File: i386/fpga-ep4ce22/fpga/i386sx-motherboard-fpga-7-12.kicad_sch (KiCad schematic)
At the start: 1 part, among them U3 (1/6) EP4CE22F17C8N

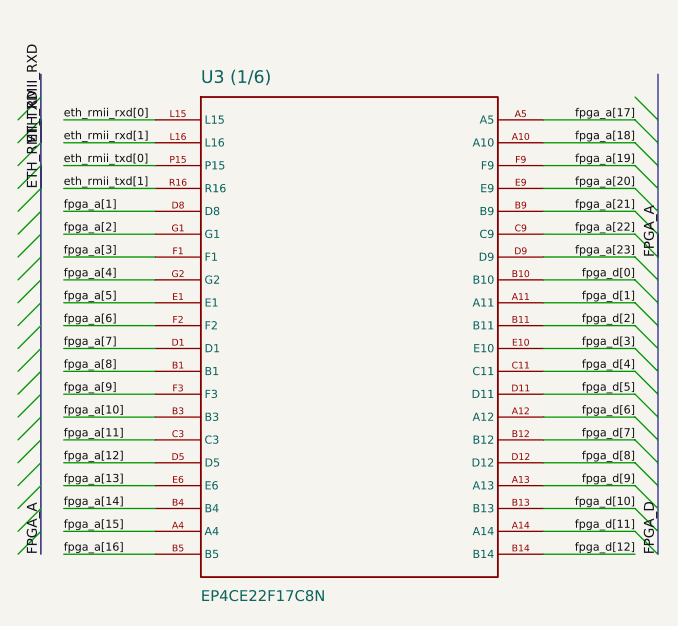
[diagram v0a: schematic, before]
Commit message: Publish the motherboards' KiCad files
From socket3@c0f6464 socket7@9205469 socket370@524f5b1 i386@bea926c
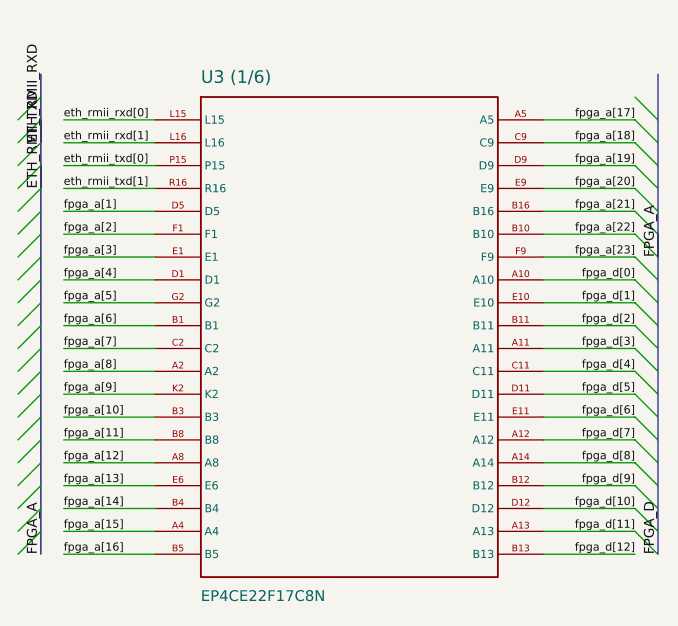
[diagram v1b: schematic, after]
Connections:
- net fpga_a[11]: now also U3 (1/6).B8; no longer U3 (1/6).C3
- net fpga_a[12]: now also U3 (1/6).A8; no longer U3 (1/6).D5
- net fpga_a[18]: now also U3 (1/6).C9; no longer U3 (1/6).A10
- net fpga_a[19]: now also U3 (1/6).D9; no longer U3 (1/6).F9
- net fpga_a[1]: now also U3 (1/6).D5; no longer U3 (1/6).D8
- net fpga_a[21]: now also U3 (1/6).B16; no longer U3 (1/6).B9
- net fpga_a[22]: now also U3 (1/6).B10; no longer U3 (1/6).C9
- net fpga_a[23]: now also U3 (1/6).F9; no longer U3 (1/6).D9
- net fpga_a[2]: now also U3 (1/6).F1; no longer U3 (1/6).G1
- net fpga_a[3]: now also U3 (1/6).E1; no longer U3 (1/6).F1
- net fpga_a[4]: now also U3 (1/6).D1; no longer U3 (1/6).G2
- net fpga_a[5]: now also U3 (1/6).G2; no longer U3 (1/6).E1
- net fpga_a[6]: now also U3 (1/6).B1; no longer U3 (1/6).F2
- net fpga_a[7]: now also U3 (1/6).C2; no longer U3 (1/6).D1
- net fpga_a[8]: now also U3 (1/6).A2; no longer U3 (1/6).B1
- net fpga_a[9]: now also U3 (1/6).K2; no longer U3 (1/6).F3
- net fpga_d[0]: now also U3 (1/6).A10; no longer U3 (1/6).B10
- net fpga_d[10]: now also U3 (1/6).D12; no longer U3 (1/6).B13
- net fpga_d[11]: now also U3 (1/6).A13; no longer U3 (1/6).A14
- net fpga_d[12]: now also U3 (1/6).B13; no longer U3 (1/6).B14
- net fpga_d[1]: now also U3 (1/6).E10; no longer U3 (1/6).A11
- net fpga_d[3]: now also U3 (1/6).A11; no longer U3 (1/6).E10
- net fpga_d[6]: now also U3 (1/6).E11; no longer U3 (1/6).A12
- net fpga_d[7]: now also U3 (1/6).A12; no longer U3 (1/6).B12
- net fpga_d[8]: now also U3 (1/6).A14; no longer U3 (1/6).D12
- net fpga_d[9]: now also U3 (1/6).B12; no longer U3 (1/6).A13
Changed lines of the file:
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@@
     (property "Reference" "U3 (1/6)" (at 44.46 17.65 0) (effects (font (size 1.4 1.4)) (justify left bottom)))
     (property "Value" "EP4CE22F17C8N" (at 44.46 73.79 0) (effects (font (size 1.2 1.2)) (justify left top)))
-    (instances (project "i386sx-motherboard" (path "/0ac398a9-1d89-4090-a36f-db7b4d3d6c0d/3610057a-4bad-4a42-9f8e-069125d0cdde" (reference "U3") (unit 1))))
+    (instances (project "i386sx-motherboard" (path "/ea05416d-ce24-4c39-9113-85b33d9a88b0/369546ea-1c13-4d92-ae2f-971c4dc578da" (reference "U3") (unit 1))))
   )
   (bus (pts (xy 26.68 16.51) (xy 26.68 24.13)) (stroke (width 0) (type default)))
